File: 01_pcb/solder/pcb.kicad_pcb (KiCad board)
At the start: 2 copper layers, 250 x 77.1 mm, 127 parts, among them J1 TYPE-C-31-M12_13, J2 AVR-ISP-6_mod, K1 KEYSW, K10 KEYSW, K11 KEYSW, K12 KEYSW, K13 KEYSW, K14 KEYSW, K15 KEYSW, K16 KEYSW, K17 KEYSW, K18 KEYSW, K19 KEYSW, K2 KEYSW, K20 KEYSW, K21 KEYSW, K22 KEYSW, K23 KEYSW, K24 KEYSW, K25 KEYSW, K26 KEYSW, K27 KEYSW, K28 KEYSW, K29 KEYSW, K3 KEYSW, K30 KEYSW, K31 KEYSW, K32 KEYSW, K33 KEYSW, K34 KEYSW, K35 KEYSW, K36 KEYSW, K37 KEYSW, K38 KEYSW, K39 KEYSW, K4 KEYSW, K40 KEYSW, K41 KEYSW, K42 KEYSW, K43 KEYSW, K44 KEYSW, K45 KEYSW, K46 KEYSW, K47 KEYSW, K48 KEYSW, K49 KEYSW, K5 KEYSW, K50 KEYSW, K51 KEYSW, K52 KEYSW, K6 KEYSW, K7 KEYSW, K8 KEYSW, K9 KEYSW, SW1 SW_PUSH, SW2 Rotary_Encoder_Switch, U1 ATMEGA32U4, U2 PRTR5V0U2X, Y1 16MHz

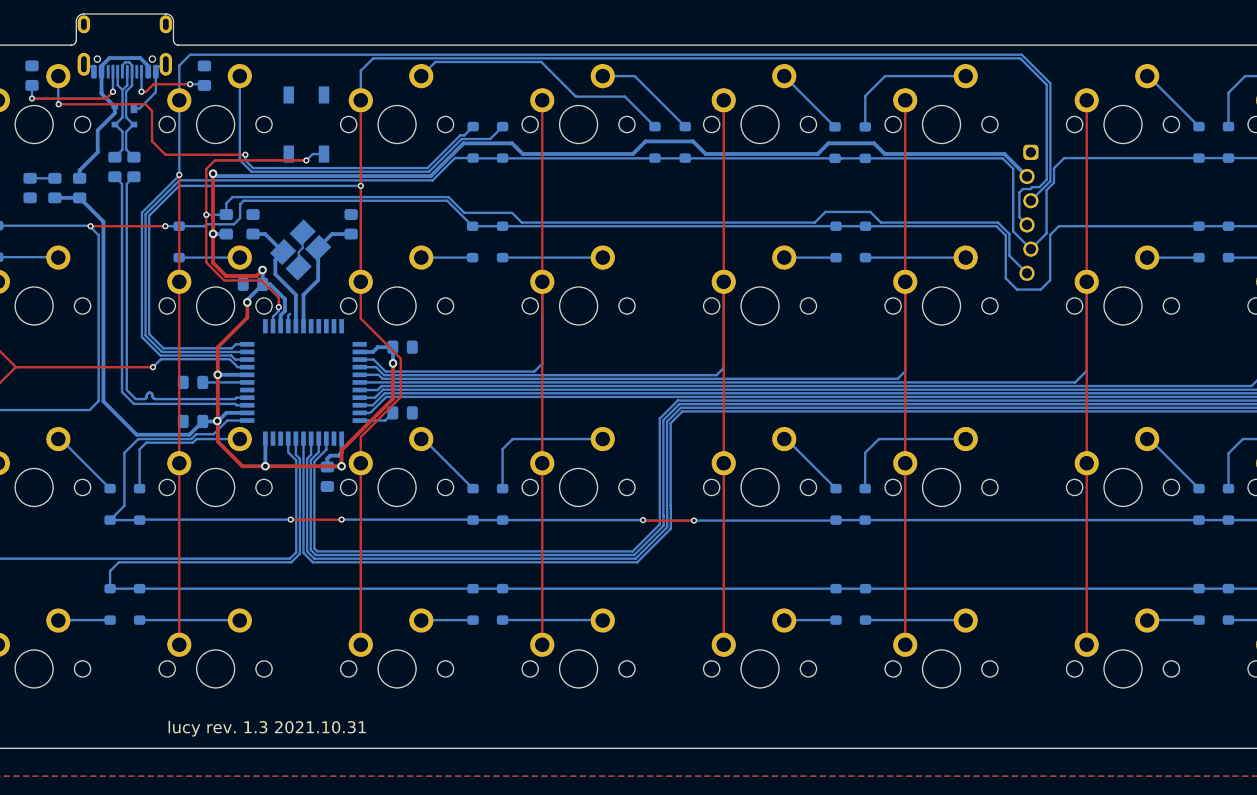
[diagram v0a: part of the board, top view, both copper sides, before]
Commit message: updated top plate
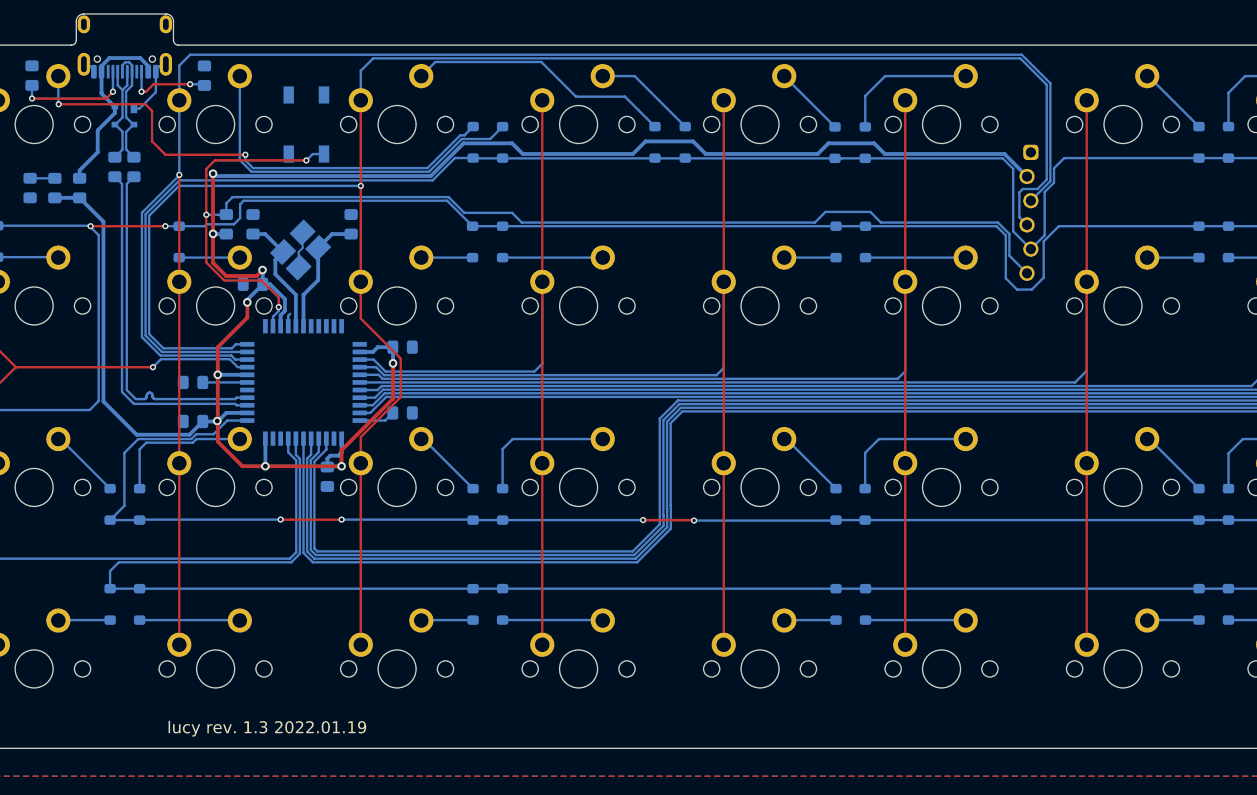
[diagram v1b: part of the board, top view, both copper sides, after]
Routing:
- net GND: track 14.5 -> 13.2 mm
- net row0: track 256.0 -> 255.3 mm
- net Net-(D13-Pad2): track 7.00 -> 6.38 mm
- net row1: track 337.1 -> 336.5 mm
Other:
- board text added: "lucy rev. 1.3 2022.01.19"
- board text removed: "lucy rev. 1.3 2021.10.31"

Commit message: 3d files
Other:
- board text added: "lucy rev. 1.3 2022.01.21"
- board text removed: "lucy rev 1.3"
- board text removed: "lucy rev. 1.3 2022.01.19"
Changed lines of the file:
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@@
     (effects (font (size 0.8 0.7) (thickness 0.15)) (justify mirror))
   )
-  (gr_text "lucy rev 1.3" (at 115.48288 116.5) (layer "B.SilkS")
+  (gr_text "lucy rev. 1.3   2022.01.21" (at 96.390625 115.95625) (layer "B.SilkS")
     (effects (font (size 1.25 1.25) (thickness 0.2)) (justify mirror))
   )
-  (gr_text "github.com/ricklicious" (at 149.13288 116.284314) (layer "B.SilkS")
+  (gr_text "github.com/ricklicious" (at 127.63288 115.740564) (layer "B.SilkS")
     (effects (font (size 1.25 1.25) (thickness 0.2)) (justify mirror))
   )
@@
     (effects (font (size 1 1) (thickness 0.15)))
   )
-  (gr_text "lucy rev. 1.3 2022.01.19" (at 111.38288 116.5) (layer "F.SilkS")
+  (gr_text "lucy rev. 1.3   2022.01.21" (at 96.29837 115.95625) (layer "F.SilkS")
     (effects (font (size 1.25 1.25) (thickness 0.2)))
   )
@@
   )
   (dimension (type aligned) (layer "Dwgs.User")
+    (pts (xy 296.465625 43.65625) (xy 320.278125 43.65625))
+    (height -3.571878)
+    (gr_text "23.8125 mm" (at 308.371875 38.934372) (layer "Dwgs.User")
+      (effects (font (size 1 1) (thickness 0.15)))
+    )
+    (format (units 3) (units_format 1) (precision 4))
+    (style (thickness 0.1) (arrow_length 1.27) (text_position_mode 0) (extension_height 0.58642) (extension_offset 0.5) keep_text_aligned)
+  )
+  (dimension (type aligned) (layer "Dwgs.User")
     (pts (xy 164.306177 45.442186) (xy 86.915617 45.442186))
     (height 7.739056)
@@
   )
   (dimension (type aligned) (layer "Dwgs.User")
-    (pts (xy 310.753125 43.65625) (xy 305.990625 43.65625))
+    (pts (xy 310.753125 43.656248) (xy 305.990625 43.656248))
     (height 1.190624)
-    (gr_text "0.1875 in" (at 308.371875 41.315626) (layer "Dwgs.User")
+    (gr_text "4.7625 mm" (at 308.371875 41.315624) (layer "Dwgs.User")
       (effects (font (size 1 1) (thickness 0.15)))
     )
-    (format (units 0) (units_format 1) (precision 4))
-    (style (thickness 0.05) (arrow_length 1.27) (text_position_mode 0) (extension_height 0.58642) (extension_offset 0) keep_text_aligned)
+    (format (units 2) (units_format 1) (precision 4))
+    (style (thickness 0.05) (arrow_length 1.27) (text_position_mode 2) (extension_height 0.58642) (extension_offset 0) keep_text_aligned)
   )
   (dimension (type aligned) (layer "Dwgs.User")

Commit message: update
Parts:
- moved J1 3.58 mm to (96.4, 44.8)
- moved U2 3.58 mm to (96.4, 48.7)
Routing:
- net DBUS-: track 13.4 -> 17.0 mm
- net DBUS+: track 12.3 -> 15.9 mm
- net VBUS: track 19.6 -> 23.2 mm
- net Net-(J1-PadA5): track 12.8 -> 16.1 mm
- net Net-(J1-PadB5): track 9.63 -> 11.5 mm
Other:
- board size 250 x 77.1 mm -> 250 x 80.7 mm

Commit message: pull old solder pcb
current solder PCB was freezing in Kicad, pulled an old one and made changes. mostly just moved USB port up
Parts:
- added H1: MountingHole, MountingHole:MountingHole_2.2mm_M2_DIN965_Pad, F.Cu at (308.4, 53.2)
- C1: footprint Capacitor_SMD:C_0805_2012Metric_Pad1.15x1.40mm_HandSolder -> Capacitor_SMD:C_0805_2012Metric_Pad1.18x1.45mm_HandSolder
- J2: footprint Keeb_footprints:PIN_HEADER_1x6_OFFSET -> Keeb_footprints:ICSP-Header
- moved J2 6.10 mm to (191.7, 56.4)
- moved U2 0.70 mm to (96.4, 49.4)
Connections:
- J1 pad A8: (no net) -> unconnected-(J1-PadA8)
- J1 pad B8: (no net) -> unconnected-(J1-PadB8)
- U1 pad 12: (no net) -> unconnected-(U1-Pad12)
- U1 pad 18: (no net) -> unconnected-(U1-Pad18)
- U1 pad 19: (no net) -> unconnected-(U1-Pad19)
- U1 pad 20: (no net) -> unconnected-(U1-Pad20)
- U1 pad 21: (no net) -> unconnected-(U1-Pad21)
- U1 pad 22: (no net) -> unconnected-(U1-Pad22)
- U1 pad 42: (no net) -> unconnected-(U1-Pad42)
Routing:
- net Net-(D1-Pad2): track 53.3 -> 55.9 mm
- net GND: track 13.2 -> 11.8 mm
- net DBUS-: track 17.0 -> 17.6 mm
- net row0: track 255.3 -> 255.8 mm
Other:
- board text added: "lucy rev 1.3.1"
- board text added: "lucy rev. 1.3.1 2022.04.11"
- board text removed: "github.com/ricklicious"
- board text removed: "lucy rev. 1.3 2022.01.21"
